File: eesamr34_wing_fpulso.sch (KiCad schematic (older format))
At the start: 12 parts, among them J3 Conn_01x02_Male, P1 SolderJumper_3_Bridged12, U2 4069

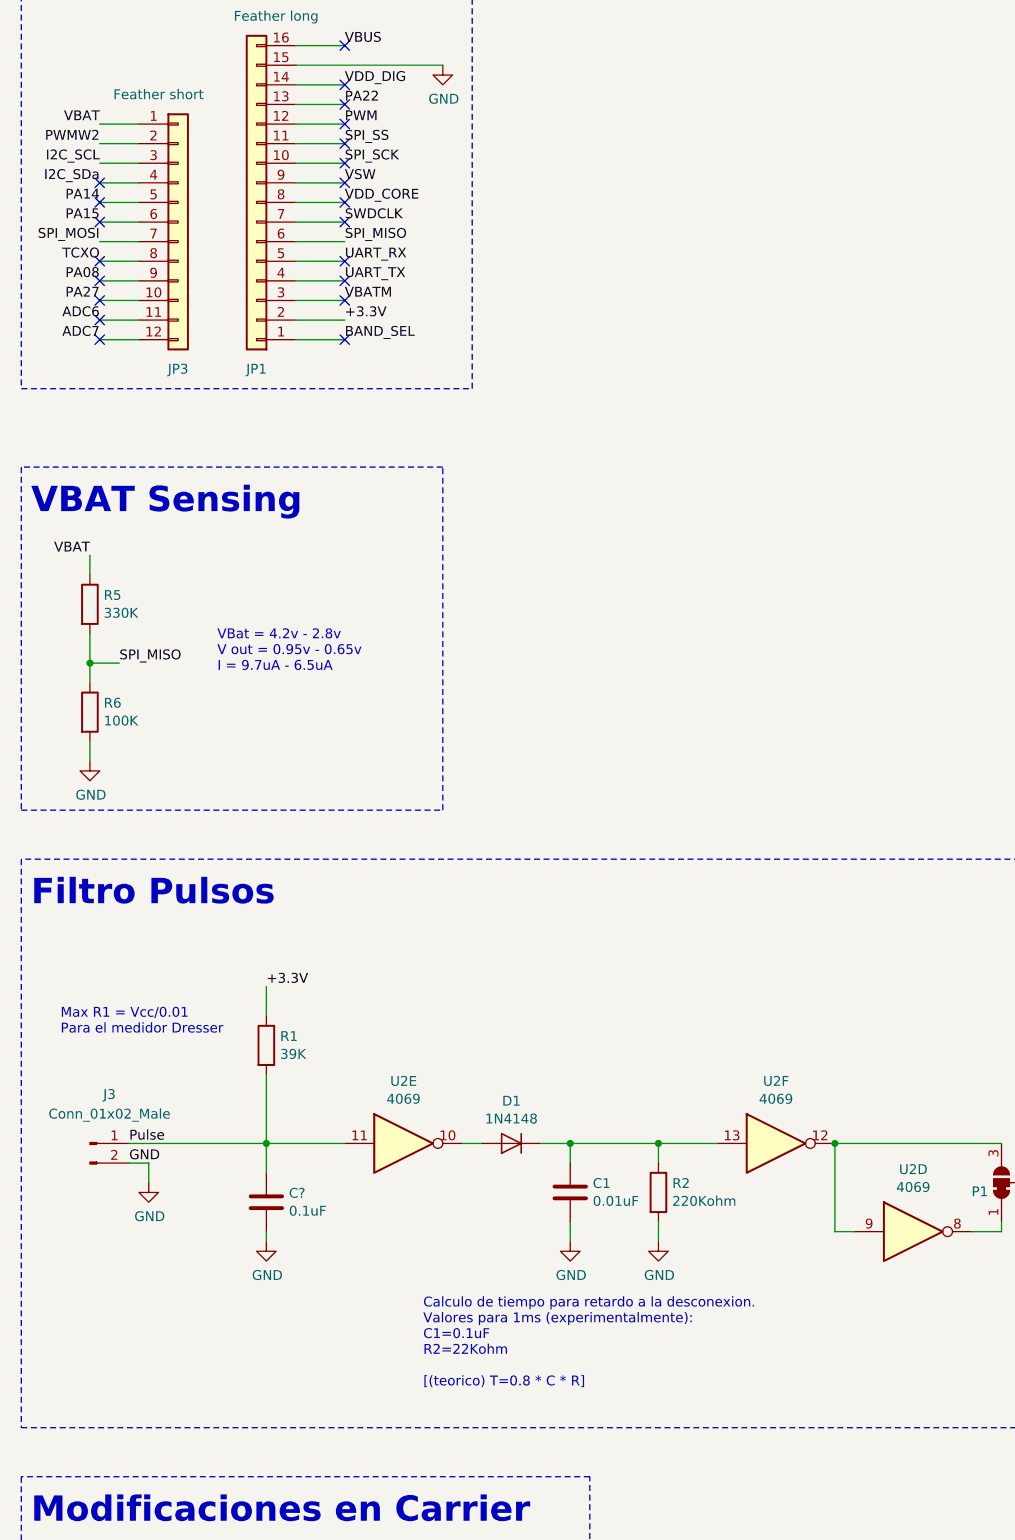
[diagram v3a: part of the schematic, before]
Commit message: quitado vbat to vcc y actualizado PCB
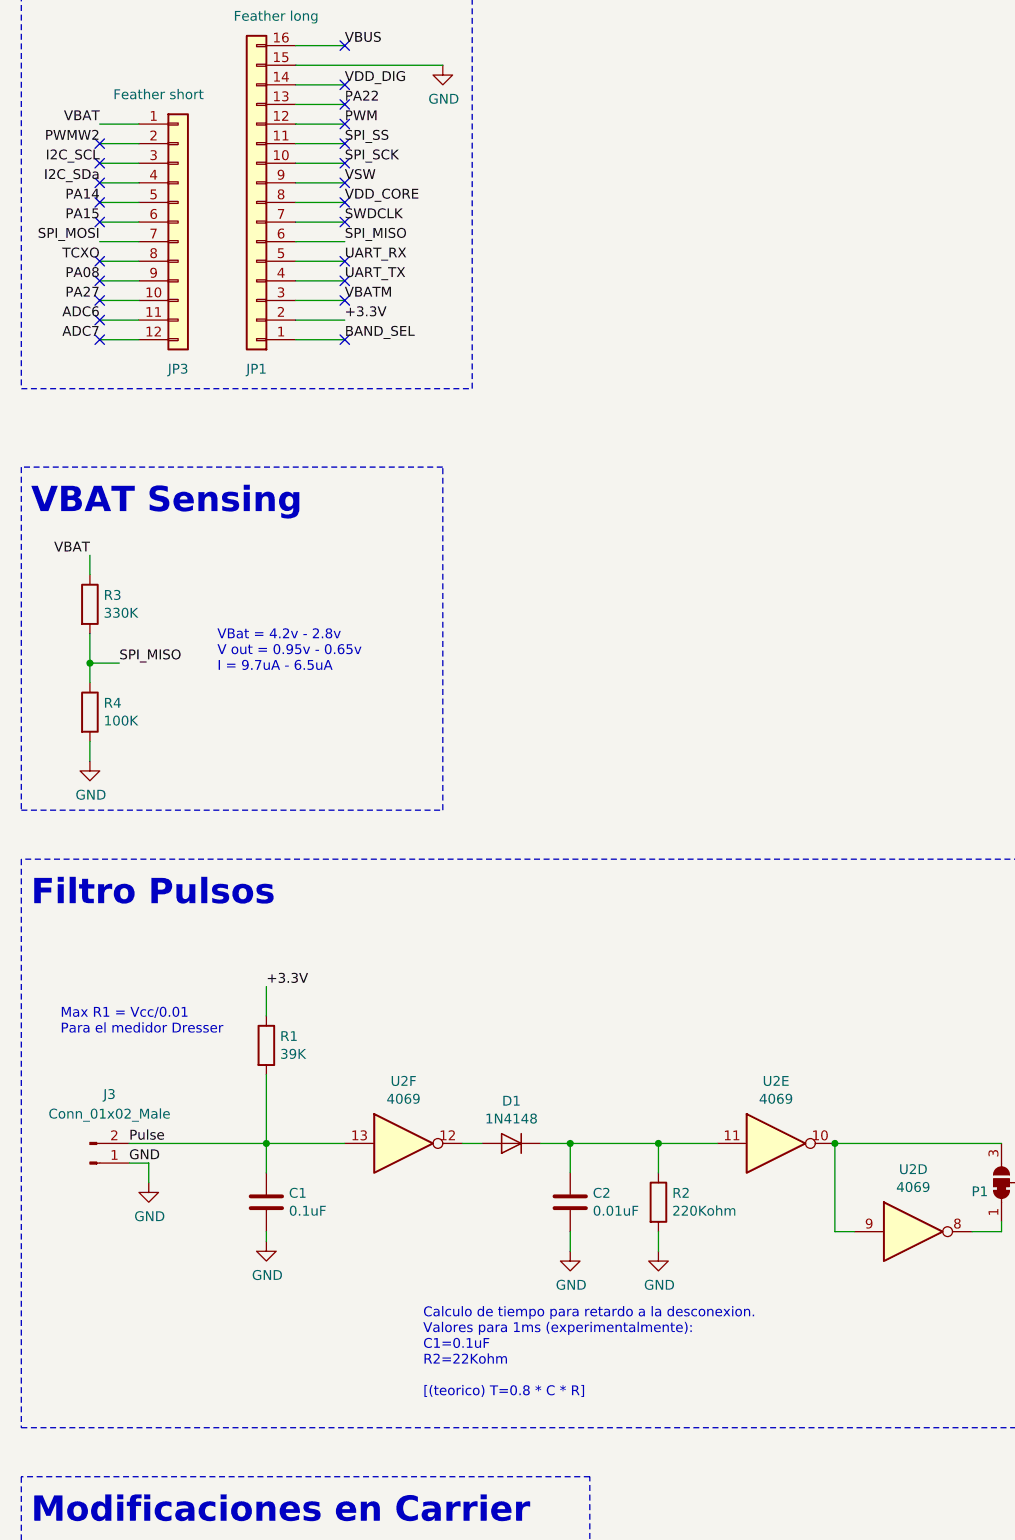
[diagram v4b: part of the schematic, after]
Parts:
- U2: footprint (none) -> Package_DIP:DIP-14_W7.62mm
- gave numbers to parts that had none: 1
- renumbered C1 to C2, R5 to R3, R6 to R4
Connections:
- net GND: now also J3.1 (Pin_1); no longer J3.2 (Pin_2)
- net Pulse: now also J3.2 (Pin_2), U2.13; no longer J3.1 (Pin_1), U2.11
- net at C2.1, D1.1 (K), R2.1: now also U2.11; no longer U2.13
- net at D1.2 (A): now also U2.12; no longer U2.10
- net at P1.3 (B), U2.9: now also U2.10; no longer U2.12
- no-connect marks 24 -> 26
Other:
- moved on the sheet: C2, R2, U2E, U2F
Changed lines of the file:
@@
 L Device:R R2
 U 1 1 5F589973
-P 3800 7100
-F 0 "R2" H 3870 7146 50  0000 L CNN
-F 1 "220Kohm" H 3870 7055 50  0000 L CNN
-F 2 "Resistor_THT:R_Axial_DIN0207_L6.3mm_D2.5mm_P10.16mm_Horizontal" V 3730 7100 50  0001 C CNN
-F 3 "~" H 3800 7100 50  0001 C CNN
-	1    3800 7100
-	1    0    0    -1
-$EndComp
-$Comp
-L Device:C C1
+P 3800 7150
+F 0 "R2" H 3870 7196 50  0000 L CNN
+F 1 "220Kohm" H 3870 7105 50  0000 L CNN
+F 2 "Resistor_THT:R_Axial_DIN0207_L6.3mm_D2.5mm_P10.16mm_Horizontal" V 3730 7150 50  0001 C CNN
+F 3 "~" H 3800 7150 50  0001 C CNN
+	1    3800 7150
+	1    0    0    -1
+$EndComp
+$Comp
+L Device:C C2
 U 1 1 5F589979
-P 3350 7100
-F 0 "C1" H 3465 7146 50  0000 L CNN
-F 1 "0.01uF" H 3465 7055 50  0000 L CNN
-F 2 "Capacitor_THT:C_Disc_D5.0mm_W2.5mm_P2.50mm" H 3388 6950 50  0001 C CNN
-F 3 "~" H 3350 7100 50  0001 C CNN
-	1    3350 7100
+P 3350 7150
+F 0 "C2" H 3465 7196 50  0000 L CNN
+F 1 "0.01uF" H 3465 7105 50  0000 L CNN
+F 2 "Capacitor_THT:C_Disc_D5.0mm_W2.5mm_P2.50mm" H 3388 7000 50  0001 C CNN
+F 3 "~" H 3350 7150 50  0001 C CNN
+	1    3350 7150
 	1    0    0    -1
 $EndComp
@@
 L power:GND #PWR0102
 U 1 1 5F58997F
-P 3350 7350
-F 0 "#PWR0102" H 3350 7100 50  0001 C CNN
-F 1 "GND" H 3355 7177 50  0000 C CNN
-F 2 "" H 3350 7350 50  0001 C CNN
-F 3 "" H 3350 7350 50  0001 C CNN
-	1    3350 7350
+P 3350 7400
+F 0 "#PWR0102" H 3350 7150 50  0001 C CNN
+F 1 "GND" H 3355 7227 50  0000 C CNN
+F 2 "" H 3350 7400 50  0001 C CNN
+F 3 "" H 3350 7400 50  0001 C CNN
+	1    3350 7400
 	1    0    0    -1
 $EndComp
@@
 L power:GND #PWR0103
 U 1 1 5F589985
-P 3800 7350
-F 0 "#PWR0103" H 3800 7100 50  0001 C CNN
-F 1 "GND" H 3805 7177 50  0000 C CNN
-F 2 "" H 3800 7350 50  0001 C CNN
-F 3 "" H 3800 7350 50  0001 C CNN
-	1    3800 7350
-	1    0    0    -1
-$EndComp
-Wire Wire Line
-	3800 6950 3800 6850
+P 3800 7400
+F 0 "#PWR0103" H 3800 7150 50  0001 C CNN
+F 1 "GND" H 3805 7227 50  0000 C CNN
+F 2 "" H 3800 7400 50  0001 C CNN
+F 3 "" H 3800 7400 50  0001 C CNN
+	1    3800 7400
+	1    0    0    -1
+$EndComp
 Wire Wire Line
 	4100 6850 3800 6850
@@
 L Connector:Conn_01x02_Male J3
 U 1 1 5F58999E
-P 900 6850
-F 0 "J3" H 1000 7100 50  0000 C CNN
-F 1 "Conn_01x02_Male" H 1000 7000 50  0000 C CNN
-F 2 "TerminalBlock:TerminalBlock_bornier-2_P5.08mm" H 900 6850 50  0001 C CNN
-F 3 "~" H 900 6850 50  0001 C CNN
-	1    900  6850
-	1    0    0    -1
+P 900 6950
+F 0 "J3" H 1000 6600 50  0000 C CNN
+F 1 "Conn_01x02_Male" H 1000 6700 50  0000 C CNN
+F 2 "TerminalBlock:TerminalBlock_bornier-2_P5.08mm" H 900 6950 50  0001 C CNN
+F 3 "~" H 900 6950 50  0001 C CNN
+	1    900  6950
+	1    0    0    1
 $EndComp
 $Comp
@@
 L 4xxx:4069 U2
 U 6 1 5F5899AA
-P 4400 6850
-F 0 "U2" H 4400 7167 50  0000 C CNN
-F 1 "4069" H 4400 7076 50  0000 C CNN
-F 2 "Package_DIP:DIP-14_W7.62mm" H 4400 6850 50  0001 C CNN
-F 3 "http://www.intersil.com/content/dam/Intersil/documents/cd40/cd4069ubms.pdf" H 4400 6850 50  0001 C CNN
-	6    4400 6850
+P 2500 6850
+F 0 "U2" H 2500 7167 50  0000 C CNN
+F 1 "4069" H 2500 7076 50  0000 C CNN
+F 2 "Package_DIP:DIP-14_W7.62mm" H 2500 6850 50  0001 C CNN
+F 3 "http://www.intersil.com/content/dam/Intersil/documents/cd40/cd4069ubms.pdf" H 2500 6850 50  0001 C CNN
+	6    2500 6850
 	1    0    0    -1
 $EndComp
@@
 Wire Wire Line
 	1800 6050 1800 6200
-Wire Wire Line
-	3350 6950 3350 6850
 Wire Wire Line
 	3350 6850 3800 6850
@@
 Text Label 1100 6950 0    50   ~ 0
 GND
-Text Notes 2600 8100 0    50   ~ 0
+Text Notes 2600 8150 0    50   ~ 0
 Calculo de tiempo para retardo a la desconexion.\nValores para 1ms (experimentalmente):\nC1=0.1uF\nR2=22Kohm\n\n[(teorico) T=0.8 * C * R]
 Text Notes 750  6300 0    50   ~ 0
@@
 Connection ~ 3350 6850
 Wire Wire Line
-	3350 7250 3350 7350
-Wire Wire Line
-	3800 7250 3800 7350
+	3350 7300 3350 7400
+Wire Wire Line
+	3800 7300 3800 7400
 Wire Wire Line
 	4700 7300 4800 7300
@@
 	900  4250 900  4400
 $Comp
-L Device:R R6
+L Device:R R4
 U 1 1 5F9E34ED
 P 900 4650
-F 0 "R6" H 970 4696 50  0000 L CNN
+F 0 "R4" H 970 4696 50  0000 L CNN
 F 1 "100K" H 970 4605 50  0000 L CNN
 F 2 "Resistor_THT:R_Axial_DIN0207_L6.3mm_D2.5mm_P10.16mm_Horizontal" V 830 4650 50  0001 C CNN
@@
 VBAT
 $Comp
-L Device:R R5
+L Device:R R3
 U 1 1 5F9D6B32
 P 900 4100
-F 0 "R5" H 970 4146 50  0000 L CNN
+F 0 "R3" H 970 4146 50  0000 L CNN
 F 1 "330K" H 970 4055 50  0000 L CNN
 F 2 "Resistor_THT:R_Axial_DIN0207_L6.3mm_D2.5mm_P10.16mm_Horizontal" V 830 4100 50  0001 C CNN
@@
 F 0 "U2" H 8900 7717 50  0000 C CNN
 F 1 "4069" H 8900 7626 50  0000 C CNN
-F 2 "" H 8900 7400 50  0001 C CNN
+F 2 "Package_DIP:DIP-14_W7.62mm" H 8900 7400 50  0001 C CNN
 F 3 "http://www.intersil.com/content/dam/Intersil/documents/cd40/cd4069ubms.pdf" H 8900 7400 50  0001 C CNN
 	2    8900 7400
@@
 F 0 "U2" H 5100 7617 50  0000 C CNN
 F 1 "4069" H 5100 7526 50  0000 C CNN
-F 2 "" H 5100 7300 50  0001 C CNN
+F 2 "Package_DIP:DIP-14_W7.62mm" H 5100 7300 50  0001 C CNN
 F 3 "http://www.intersil.com/content/dam/Intersil/documents/cd40/cd4069ubms.pdf" H 5100 7300 50  0001 C CNN
 	4    5100 7300
@@
 L 4xxx:4069 U2
 U 5 1 5F93F0BA
-P 2500 6850
-F 0 "U2" H 2500 7167 50  0000 C CNN
-F 1 "4069" H 2500 7076 50  0000 C CNN
-F 2 "" H 2500 6850 50  0001 C CNN
-F 3 "http://www.intersil.com/content/dam/Intersil/documents/cd40/cd4069ubms.pdf" H 2500 6850 50  0001 C CNN
-	5    2500 6850
+P 4400 6850
+F 0 "U2" H 4400 7167 50  0000 C CNN
+F 1 "4069" H 4400 7076 50  0000 C CNN
+F 2 "Package_DIP:DIP-14_W7.62mm" H 4400 6850 50  0001 C CNN
+F 3 "http://www.intersil.com/content/dam/Intersil/documents/cd40/cd4069ubms.pdf" H 4400 6850 50  0001 C CNN
+	5    4400 6850
 	1    0    0    -1
 $EndComp
@@
 NoConn ~ 2200 1250
 $Comp
-L Device:C C?
+L Device:C C1
 U 1 1 5FA241A0
 P 1800 7150
-F 0 "C?" H 1915 7196 50  0000 L CNN
+F 0 "C1" H 1915 7196 50  0000 L CNN
 F 1 "0.1uF" H 1915 7105 50  0000 L CNN
 F 2 "Capacitor_THT:C_Disc_D5.0mm_W2.5mm_P2.50mm" H 1838 7000 50  0001 C CNN
@@
 $EndComp
 $Comp
-L power:GND #PWR?
+L power:GND #PWR0106
 U 1 1 5FA26127
 P 1800 7350
-F 0 "#PWR?" H 1800 7100 50  0001 C CNN
+F 0 "#PWR0106" H 1800 7100 50  0001 C CNN
 F 1 "GND" H 1805 7177 50  0000 C CNN
 F 2 "" H 1800 7350 50  0001 C CNN
@@
 Wire Wire Line
 	1800 7300 1800 7350
+Wire Wire Line
+	3350 6850 3350 7000
+Wire Wire Line
+	3800 6850 3800 7000
+NoConn ~ 950  1750
+NoConn ~ 950  1850
 $EndSCHEMATC

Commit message: Tercer borne permite alimentar el nodo usando 5v
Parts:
- removed J3: Conn_01x02_Male, TerminalBlock:TerminalBlock_bornier-2_P5.08mm, symbol Connector:Conn_01x02_Male
- added J1: Conn_01x03_Male, TerminalBlock:TerminalBlock_bornier-3_P5.08mm, symbol Connector:Conn_01x03_Male
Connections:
- net GND: now also J1.1 (Pin_1)
- net Pulse: now also J1.2 (Pin_2)
- net VBUS: now also J1.3 (Pin_3)
- no-connect marks 26 -> 25
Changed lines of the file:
@@
 Connection ~ 3800 6850
-$Comp
-L Connector:Conn_01x02_Male J3
-U 1 1 5F58999E
-P 900 6950
-F 0 "J3" H 1000 6600 50  0000 C CNN
-F 1 "Conn_01x02_Male" H 1000 6700 50  0000 C CNN
-F 2 "TerminalBlock:TerminalBlock_bornier-2_P5.08mm" H 900 6950 50  0001 C CNN
-F 3 "~" H 900 6950 50  0001 C CNN
-	1    900  6950
-	1    0    0    1
-$EndComp
 $Comp
 L 4xxx:4069 U2
@@
 Text Label 5950 7050 0    50   ~ 0
 SPI_MOSI
-NoConn ~ 2200 1250
 $Comp
 L Device:C C1
@@
 NoConn ~ 950  1750
 NoConn ~ 950  1850
+$Comp
+L Connector:Conn_01x03_Male J1
+U 1 1 5FBAF14F
+P 900 6850
+F 0 "J1" H 872 6782 50  0000 R CNN
+F 1 "Conn_01x03_Male" H 872 6873 50  0000 R CNN
+F 2 "TerminalBlock:TerminalBlock_bornier-3_P5.08mm" H 900 6850 50  0001 C CNN
+F 3 "~" H 900 6850 50  0001 C CNN
+	1    900  6850
+	1    0    0    1
+$EndComp
+Wire Wire Line
+	1150 6750 1100 6750
+Text Label 1150 6750 0    50   ~ 0
+VBUS
 $EndSCHEMATC
